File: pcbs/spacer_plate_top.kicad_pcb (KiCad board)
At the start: 2 copper layers, 73 x 111 mm, 0 parts

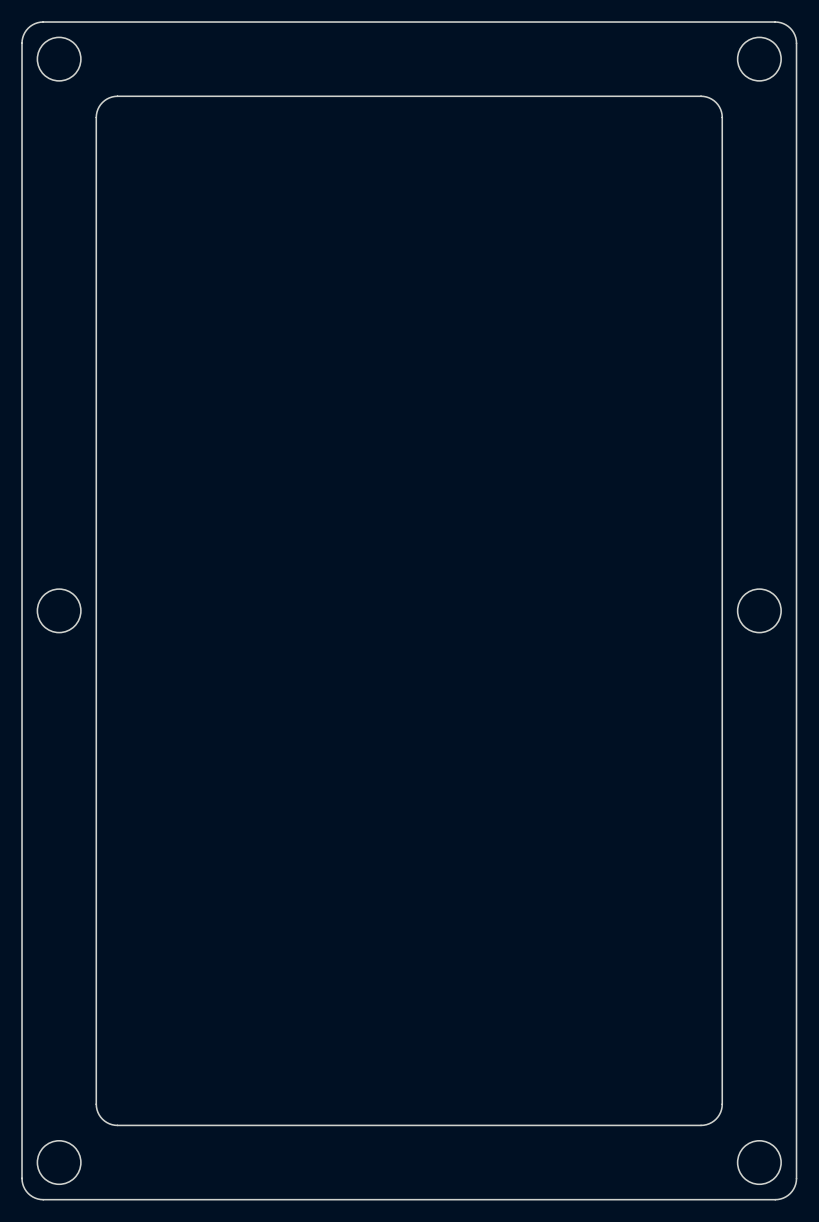
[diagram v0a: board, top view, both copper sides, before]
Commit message: Update MX switch footprint
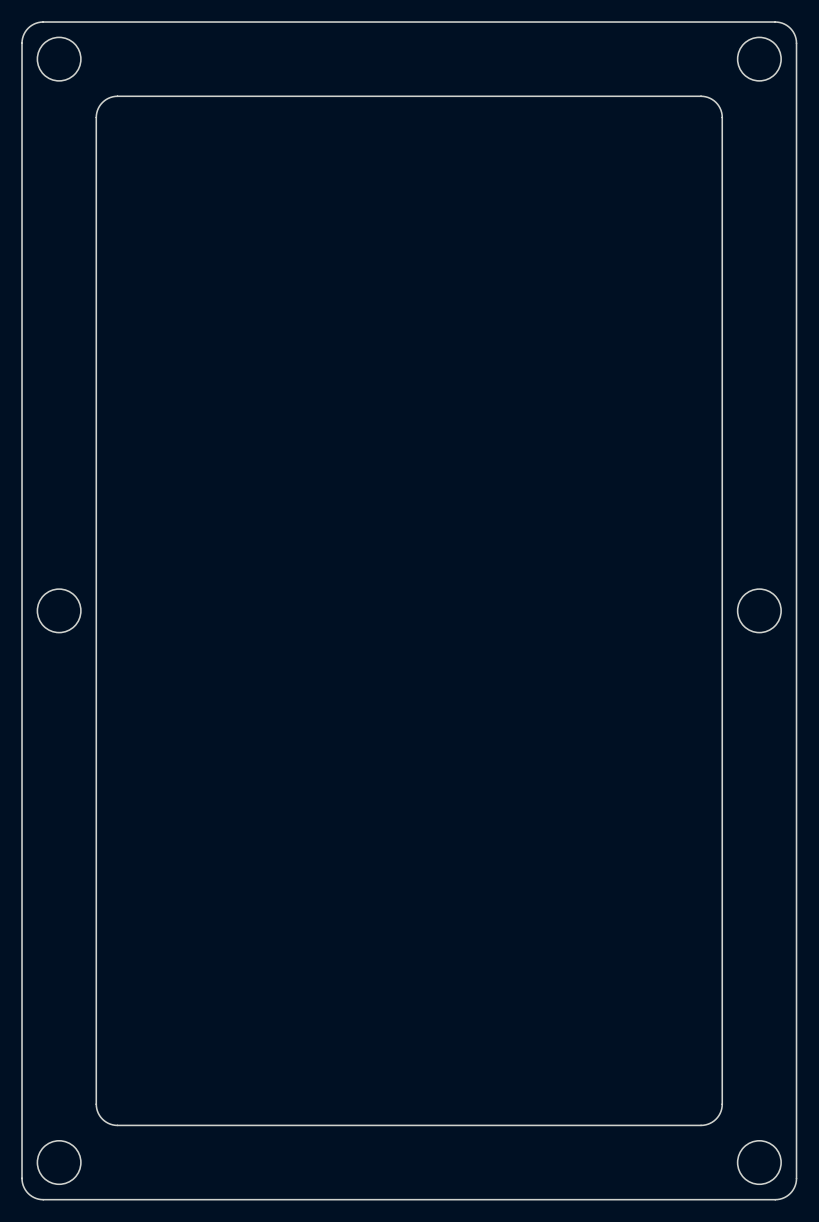
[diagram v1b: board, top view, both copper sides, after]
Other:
- net class Default removed
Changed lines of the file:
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@@
-(kicad_pcb (version 20171130) (host pcbnew 5.1.6)
-  (page A3)
+(kicad_pcb
+  (version 20240108)
+  (generator "ergogen")
+  (generator_version "4.1.0")
+  (general
+    (thickness 1.6)
+    (legacy_teardrops no)
+  )
+  (paper "A3")
   (title_block
     (title "spacer_plate_top")
+    (date "2024-11-14")
     (rev "0.1")
     (company "ceoloide")
   )
-  (general
-    (thickness 1.6)
-  )
   (layers
-    (0 F.Cu signal)
-    (31 B.Cu signal)
-    (32 B.Adhes user)
-    (33 F.Adhes user)
-    (34 B.Paste user)
-    (35 F.Paste user)
-    (36 B.SilkS user)
-    (37 F.SilkS user)
-    (38 B.Mask user)
-    (39 F.Mask user)
-    (40 Dwgs.User user)
-    (41 Cmts.User user)
-    (42 Eco1.User user)
-    (43 Eco2.User user)
-    (44 Edge.Cuts user)
-    (45 Margin user)
-    (46 B.CrtYd user)
-    (47 F.CrtYd user)
-    (48 B.Fab user)
-    (49 F.Fab user)
+    (0 "F.Cu" signal)
+    (31 "B.Cu" signal)
+    (32 "B.Adhes" user "B.Adhesive")
+    (33 "F.Adhes" user "F.Adhesive")
+    (34 "B.Paste" user)
+    (35 "F.Paste" user)
+    (36 "B.SilkS" user "B.Silkscreen")
+    (37 "F.SilkS" user "F.Silkscreen")
+    (38 "B.Mask" user)
+    (39 "F.Mask" user)
+    (40 "Dwgs.User" user "User.Drawings")
+    (41 "Cmts.User" user "User.Comments")
+    (42 "Eco1.User" user "User.Eco1")
+    (43 "Eco2.User" user "User.Eco2")
+    (44 "Edge.Cuts" user)
+    (45 "Margin" user)
+    (46 "B.CrtYd" user "B.Courtyard")
+    (47 "F.CrtYd" user "F.Courtyard")
+    (48 "B.Fab" user)
+    (49 "F.Fab" user)
   )
   (setup
-    (last_trace_width 0.25)
-    (trace_clearance 0.2)
-    (zone_clearance 0.508)
-    (zone_45_only no)
-    (trace_min 0.2)
-    (via_size 0.8)
-    (via_drill 0.4)
-    (via_min_size 0.4)
-    (via_min_drill 0.3)
-    (uvia_size 0.3)
-    (uvia_drill 0.1)
-    (uvias_allowed no)
-    (uvia_min_size 0.2)
-    (uvia_min_drill 0.1)
-    (edge_width 0.05)
-    (segment_width 0.2)
-    (pcb_text_width 0.3)
-    (pcb_text_size 1.5 1.5)
-    (mod_edge_width 0.12)
-    (mod_text_size 1 1)
-    (mod_text_width 0.15)
-    (pad_size 1.524 1.524)
-    (pad_drill 0.762)
     (pad_to_mask_clearance 0.05)
-    (aux_axis_origin 0 0)
-    (visible_elements FFFFFF7F)
+    (allow_soldermask_bridges_in_footprints no)
     (pcbplotparams
-      (layerselection 0x010fc_ffffffff)
-      (usegerberextensions false)
-      (usegerberattributes true)
-      (usegerberadvancedattributes true)
-      (creategerberjobfile true)
-      (excludeedgelayer true)
-      (linewidth 0.100000)
-      (plotframeref false)
-      (viasonmask false)
+      (layerselection 0x00010fc_ffffffff)
+      (plot_on_all_layers_selection 0x0000000_00000000)
+      (disableapertmacros no)
+      (usegerberextensions no)
+      (usegerberattributes yes)
+      (usegerberadvancedattributes yes)
+      (creategerberjobfile yes)
+      (dashed_line_dash_ratio 12.000000)
+      (dashed_line_gap_ratio 3.000000)
+      (svgprecision 4)
+      (plotframeref no)
+      (viasonmask no)
       (mode 1)
-      (useauxorigin false)
+      (useauxorigin no)
       (hpglpennumber 1)
       (hpglpenspeed 20)
       (hpglpendiameter 15.000000)
-      (psnegative false)
-      (psa4output false)
-      (plotreference true)
-      (plotvalue true)
-      (plotinvisibletext false)
-      (padsonsilk false)
-      (subtractmaskfromsilk false)
+      (pdf_front_fp_property_popups yes)
+      (pdf_back_fp_property_popups yes)
+      (dxfpolygonmode yes)
+      (dxfimperialunits yes)
+      (dxfusepcbnewfont yes)
+      (psnegative no)
+      (psa4output no)
+      (plotreference yes)
+      (plotvalue yes)
+      (plotfptext yes)
+      (plotinvisibletext no)
+      (sketchpadsonfab no)
+      (subtractmaskfromsilk no)
       (outputformat 1)
-      (mirror false)
+      (mirror no)
       (drillshape 1)
       (scaleselection 1)
-      (outputdirectory ""))
+      (outputdirectory "")
+    )
   )
   (net 0 "")
-  (net_class Default "This is the default net class."
-    (clearance 0.2)
-    (trace_width 0.25)
-    (via_dia 0.8)
-    (via_drill 0.4)
-    (uvia_dia 0.3)
-    (uvia_drill 0.1)
-    (add_net "")
-  )
-  (gr_line (start 44.5 142.5) (end 113.5 142.5) (angle 90) (layer Edge.Cuts) (width 0.15))
-(gr_line (start 115.5 140.5) (end 115.5 33.5) (angle 90) (layer Edge.Cuts) (width 0.15))
-(gr_line (start 44.5 31.5) (end 113.5 31.5) (angle 90) (layer Edge.Cuts) (width 0.15))
-(gr_line (start 42.5 140.5) (end 42.5 33.5) (angle 90) (layer Edge.Cuts) (width 0.15))
-(gr_arc (start 113.5 140.5) (end 113.5 142.5) (angle -90) (layer Edge.Cuts) (width 0.15))
-(gr_arc (start 113.5 33.5) (end 115.5 33.5) (angle -90) (layer Edge.Cuts) (width 0.15))
-(gr_arc (start 44.5 33.5) (end 44.5 31.5) (angle -90) (layer Edge.Cuts) (width 0.15))
-(gr_arc (start 44.5 140.5) (end 42.5 140.5) (angle -90) (layer Edge.Cuts) (width 0.15))
-(gr_line (start 51.5 135.5) (end 106.5 135.5) (angle 90) (layer Edge.Cuts) (width 0.15))
-(gr_arc (start 106.5 133.5) (end 106.5 135.5) (angle -90) (layer Edge.Cuts) (width 0.15))
-(gr_line (start 108.5 133.5) (end 108.5 40.5) (angle 90) (layer Edge.Cuts) (width 0.15))
-(gr_arc (start 106.5 40.5) (end 108.5 40.5) (angle -90) (layer Edge.Cuts) (width 0.15))
-(gr_line (start 106.5 38.5) (end 51.5 38.5) (angle 90) (layer Edge.Cuts) (width 0.15))
-(gr_arc (start 51.5 40.5) (end 51.5 38.5) (angle -90) (layer Edge.Cuts) (width 0.15))
-(gr_line (start 49.5 40.5) (end 49.5 133.5) (angle 90) (layer Edge.Cuts) (width 0.15))
-(gr_arc (start 51.5 133.5) (end 49.5 133.5) (angle -90) (layer Edge.Cuts) (width 0.15))
-(gr_circle (center 46 35) (end 48.05 35) (layer Edge.Cuts) (width 0.15))
-(gr_circle (center 112 35) (end 114.05 35) (layer Edge.Cuts) (width 0.15))
-(gr_circle (center 46 87) (end 48.05 87) (layer Edge.Cuts) (width 0.15))
-(gr_circle (center 112 87) (end 114.05 87) (layer Edge.Cuts) (width 0.15))
-(gr_circle (center 46 139) (end 48.05 139) (layer Edge.Cuts) (width 0.15))
-(gr_circle (center 112 139) (end 114.05 139) (layer Edge.Cuts) (width 0.15))
+  (gr_line (start 44.5 142.5) (end 113.5 142.5) (layer Edge.Cuts) (stroke (width 0.15) (type default)))
+(gr_line (start 115.5 140.5) (end 115.5 33.5) (layer Edge.Cuts) (stroke (width 0.15) (type default)))
+(gr_line (start 44.5 31.5) (end 113.5 31.5) (layer Edge.Cuts) (stroke (width 0.15) (type default)))
+(gr_line (start 42.5 140.5) (end 42.5 33.5) (layer Edge.Cuts) (stroke (width 0.15) (type default)))
+(gr_arc (start 113.5 142.5) (mid 114.9142136 141.9142136) (end 115.5 140.5) (layer Edge.Cuts) (stroke (width 0.15) (type default)))
+(gr_arc (start 115.5 33.5) (mid 114.9142136 32.0857864) (end 113.5 31.5) (layer Edge.Cuts) (stroke (width 0.15) (type default)))
+(gr_arc (start 44.5 31.5) (mid 43.0857864 32.0857864) (end 42.5 33.5) (layer Edge.Cuts) (stroke (width 0.15) (type default)))
+(gr_arc (start 42.5 140.5) (mid 43.0857864 141.9142136) (end 44.5 142.5) (layer Edge.Cuts) (stroke (width 0.15) (type default)))
+(gr_line (start 51.5 135.5) (end 106.5 135.5) (layer Edge.Cuts) (stroke (width 0.15) (type default)))
+(gr_arc (start 106.5 135.5) (mid 107.9142136 134.9142136) (end 108.5 133.5) (layer Edge.Cuts) (stroke (width 0.15) (type default)))
+(gr_line (start 108.5 133.5) (end 108.5 40.5) (layer Edge.Cuts) (stroke (width 0.15) (type default)))
+(gr_arc (start 108.5 40.5) (mid 107.9142136 39.0857864) (end 106.5 38.5) (layer Edge.Cuts) (stroke (width 0.15) (type default)))
+(gr_line (start 106.5 38.5) (end 51.5 38.5) (layer Edge.Cuts) (stroke (width 0.15) (type default)))
+(gr_arc (start 51.5 38.5) (mid 50.0857864 39.0857864) (end 49.5 40.5) (layer Edge.Cuts) (stroke (width 0.15) (type default)))
+(gr_line (start 49.5 40.5) (end 49.5 133.5) (layer Edge.Cuts) (stroke (width 0.15) (type default)))
+(gr_arc (start 49.5 133.5) (mid 50.0857864 134.9142136) (end 51.5 135.5) (layer Edge.Cuts) (stroke (width 0.15) (type default)))
+(gr_circle (center 46 35) (end 48.05 35) (layer Edge.Cuts) (stroke (width 0.15) (type default)) (fill none))
+(gr_circle (center 112 35) (end 114.05 35) (layer Edge.Cuts) (stroke (width 0.15) (type default)) (fill none))
+(gr_circle (center 46 87) (end 48.05 87) (layer Edge.Cuts) (stroke (width 0.15) (type default)) (fill none))
+(gr_circle (center 112 87) (end 114.05 87) (layer Edge.Cuts) (stroke (width 0.15) (type default)) (fill none))
+(gr_circle (center 46 139) (end 48.05 139) (layer Edge.Cuts) (stroke (width 0.15) (type default)) (fill none))
+(gr_circle (center 112 139) (end 114.05 139) (layer Edge.Cuts) (stroke (width 0.15) (type default)) (fill none))
 )
